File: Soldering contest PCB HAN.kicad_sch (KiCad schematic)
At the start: 11 parts, among them J1 Screw_Terminal_01x02, Q1 2N3904, Q2 2N3904

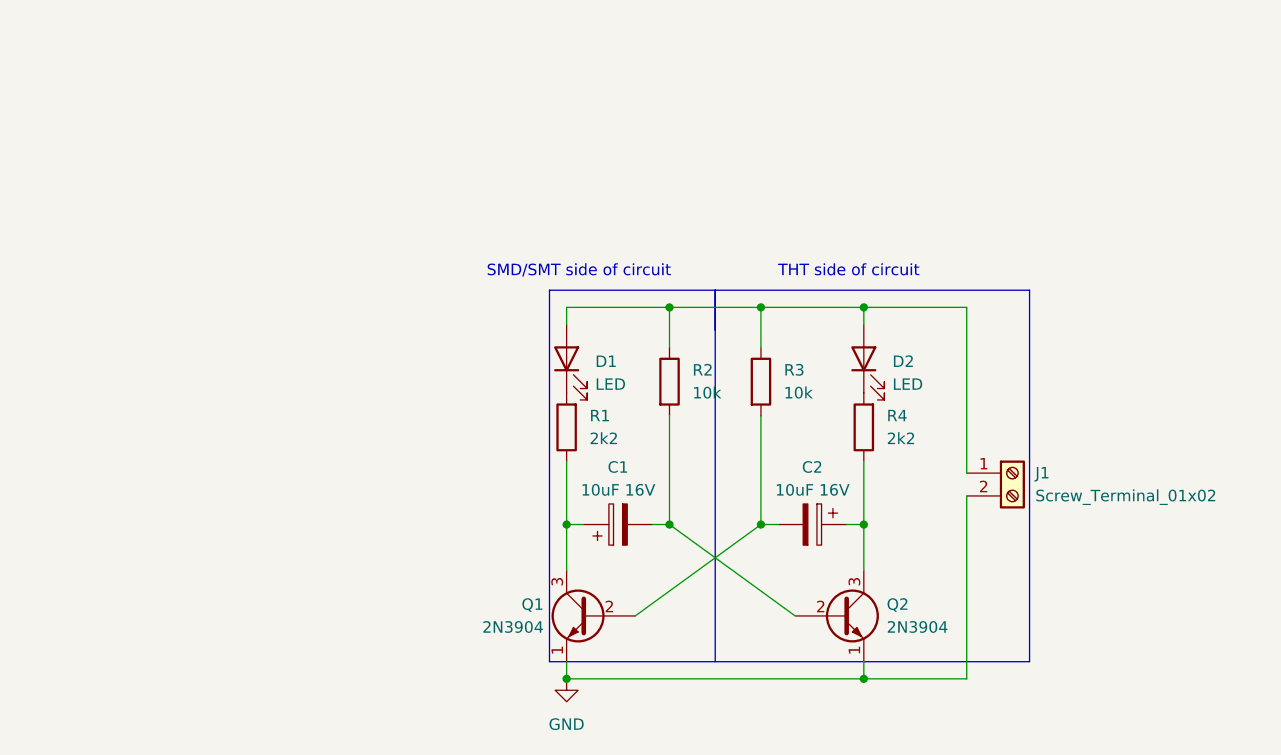
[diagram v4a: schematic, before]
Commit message: improved schematic board size
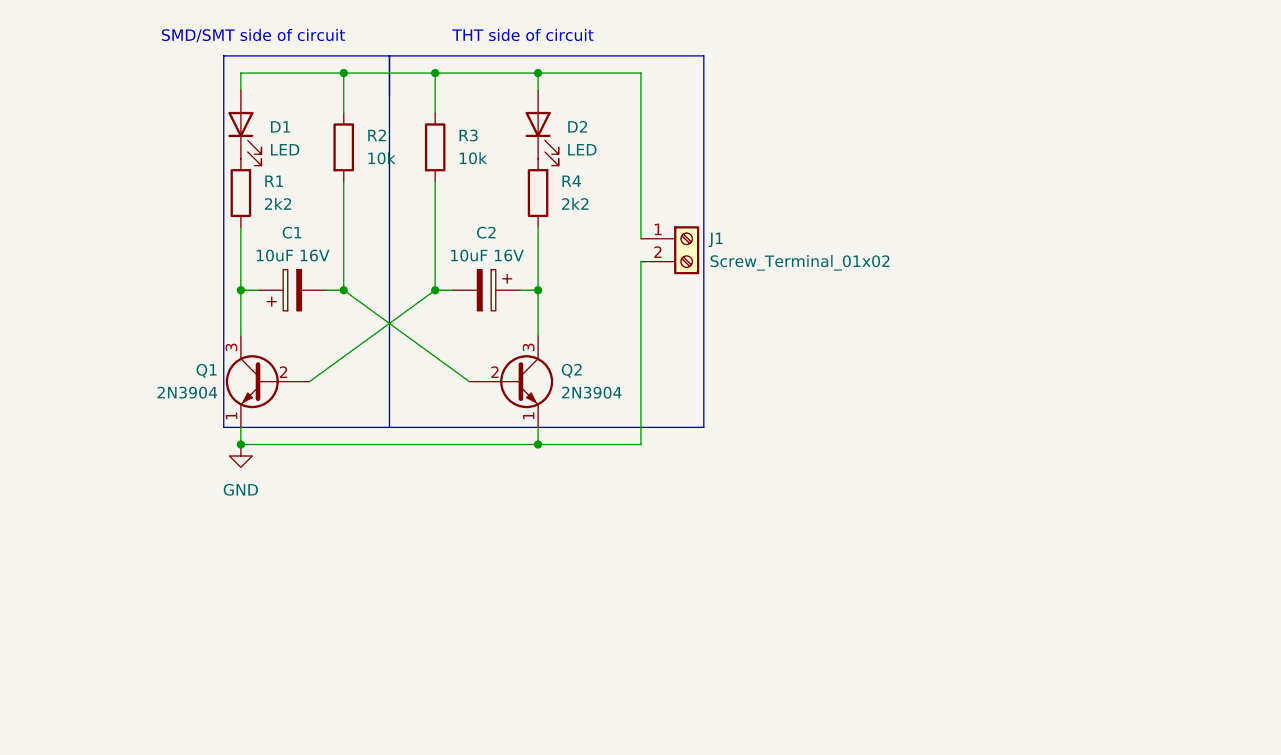
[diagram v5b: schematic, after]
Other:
- moved on the sheet: C1, C2, D1, D2, J1, Q1, Q2, R1, R2, R3, R4

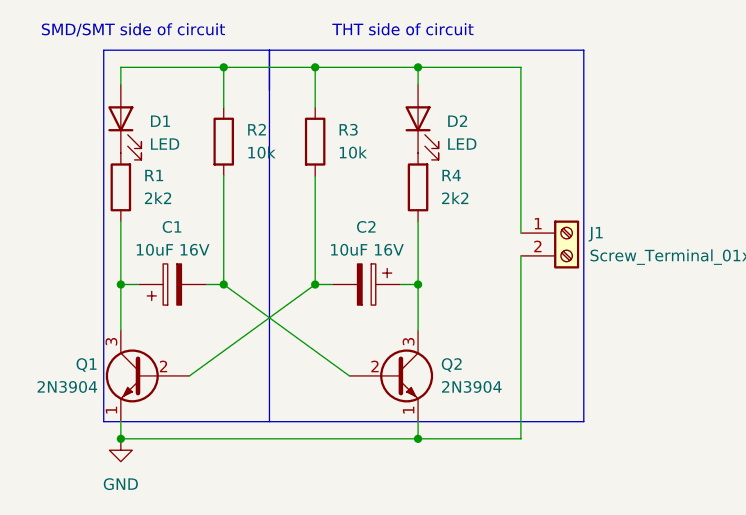
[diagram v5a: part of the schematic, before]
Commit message: replaced q1 footprint
replaced with sot23 handsolderable
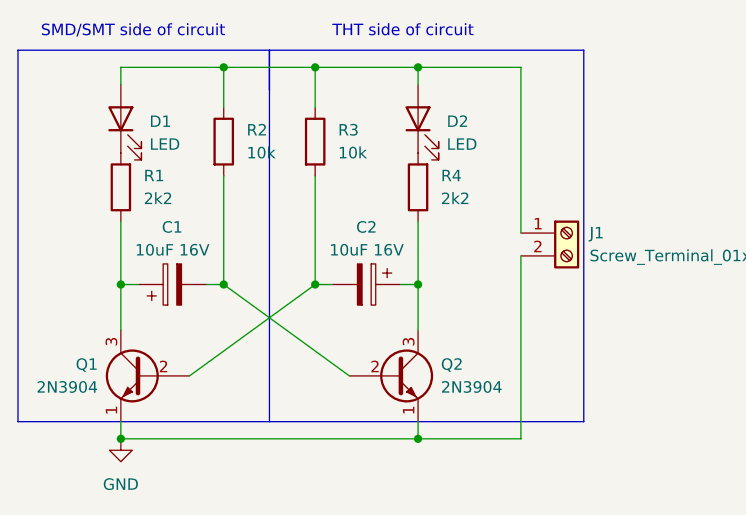
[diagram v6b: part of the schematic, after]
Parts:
- Q1: footprint Package_TO_SOT_THT:TO-92_Inline -> Package_TO_SOT_SMD:SOT-23_Handsoldering
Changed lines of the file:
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@@
   (junction (at 89.535 73.025) (diameter 0) (color 0 0 0 0)
   )
-  (polyline (pts (xy 94.615 46.99) (xy 76.2 46.99))
+  (polyline (pts (xy 94.615 46.99) (xy 66.675 46.99))
     (stroke (width 0) (type default) (color 0 0 0 0))
   )
@@
     (stroke (width 0) (type default) (color 0 0 0 0))
   )
-  (polyline (pts (xy 76.2 88.265) (xy 129.54 88.265))
+  (polyline (pts (xy 66.675 88.265) (xy 129.54 88.265))
     (stroke (width 0) (type default) (color 0 0 0 0))
   )
@@
     (stroke (width 0) (type default) (color 0 0 0 0))
   )
-  (polyline (pts (xy 76.2 46.99) (xy 76.2 88.265))
+  (polyline (pts (xy 66.675 46.99) (xy 66.675 88.265))
     (stroke (width 0) (type default) (color 0 0 0 0))
   )
@@
       (effects (font (size 1.27 1.27)) (justify left))
     )
-    (property "Footprint" "Package_TO_SOT_THT:TO-92_Inline" (id 2) (at 75.565 85.09 0)
+    (property "Footprint" "Package_TO_SOT_SMD:SOT-23_Handsoldering" (id 2) (at 75.565 85.09 0)
       (effects (font (size 1.27 1.27) italic) (justify left) hide)
     )
@@
     )
     (path "/6b424259-f8a0-4482-996c-adc9565aa863"
-      (reference "Q1") (unit 1) (value "2N3904") (footprint "Package_TO_SOT_THT:TO-92_Inline")
+      (reference "Q1") (unit 1) (value "2N3904") (footprint "Package_TO_SOT_SMD:SOT-23_Handsoldering")
     )
     (path "/0fd58cd3-0637-4e39-b339-0859c358a065"

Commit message: changed r3 footprint
smaller, so it's clear that it has to be soldered vertically
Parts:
- Q2: footprint Package_TO_SOT_THT:TO-92_Inline -> Package_TO_SOT_THT:TO-92_Inline_Wide
- R3: footprint Resistor_THT:R_Axial_DIN0207_L6.3mm_D2.5mm_P5.08mm_Vertical -> Resistor_THT:R_Axial_DIN0204_L3.6mm_D1.6mm_P2.54mm_Vertical
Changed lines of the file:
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@@
       (effects (font (size 1.27 1.27)) (justify left))
     )
-    (property "Footprint" "Package_TO_SOT_THT:TO-92_Inline" (id 2) (at 113.665 85.09 0)
+    (property "Footprint" "Package_TO_SOT_THT:TO-92_Inline_Wide" (id 2) (at 113.665 85.09 0)
       (effects (font (size 1.27 1.27) italic) (justify left) hide)
     )
@@
       (effects (font (size 1.27 1.27)) (justify left))
     )
-    (property "Footprint" "Resistor_THT:R_Axial_DIN0207_L6.3mm_D2.5mm_P5.08mm_Vertical" (id 2) (at 97.917 57.15 90)
+    (property "Footprint" "Resistor_THT:R_Axial_DIN0204_L3.6mm_D1.6mm_P2.54mm_Vertical" (id 2) (at 97.917 57.15 90)
       (effects (font (size 1.27 1.27)) hide)
     )
@@
     )
     (path "/0fd58cd3-0637-4e39-b339-0859c358a065"
-      (reference "Q2") (unit 1) (value "2N3904") (footprint "Package_TO_SOT_THT:TO-92_Inline")
+      (reference "Q2") (unit 1) (value "2N3904") (footprint "Package_TO_SOT_THT:TO-92_Inline_Wide")
     )
     (path "/d18fc897-0878-42f5-b8a2-449363703de6"
@@
     )
     (path "/5fd75fa8-c971-4180-8d4d-419bf5fd463a"
-      (reference "R3") (unit 1) (value "10k") (footprint "Resistor_THT:R_Axial_DIN0207_L6.3mm_D2.5mm_P5.08mm_Vertical")
+      (reference "R3") (unit 1) (value "10k") (footprint "Resistor_THT:R_Axial_DIN0204_L3.6mm_D1.6mm_P2.54mm_Vertical")
     )
     (path "/22a04216-54cb-44fe-9b76-e181b36e1a9f"

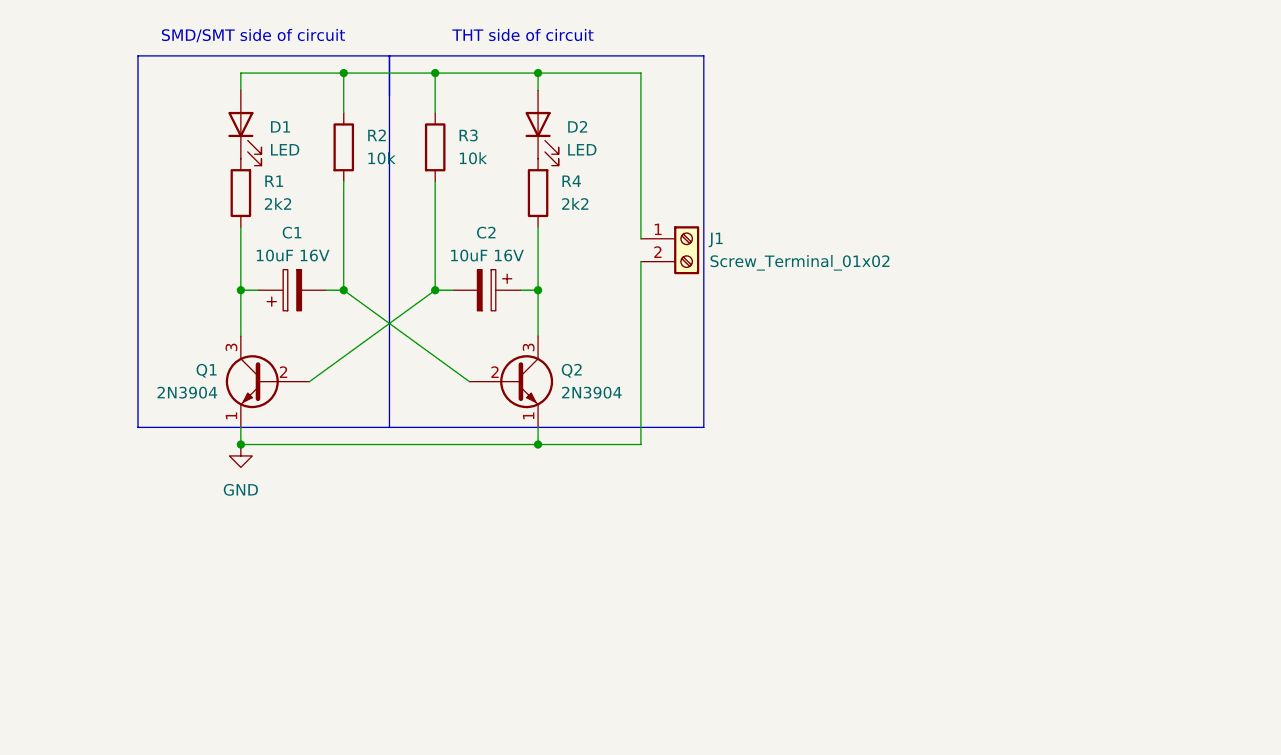
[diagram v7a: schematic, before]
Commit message: add bat, switch changed schematic
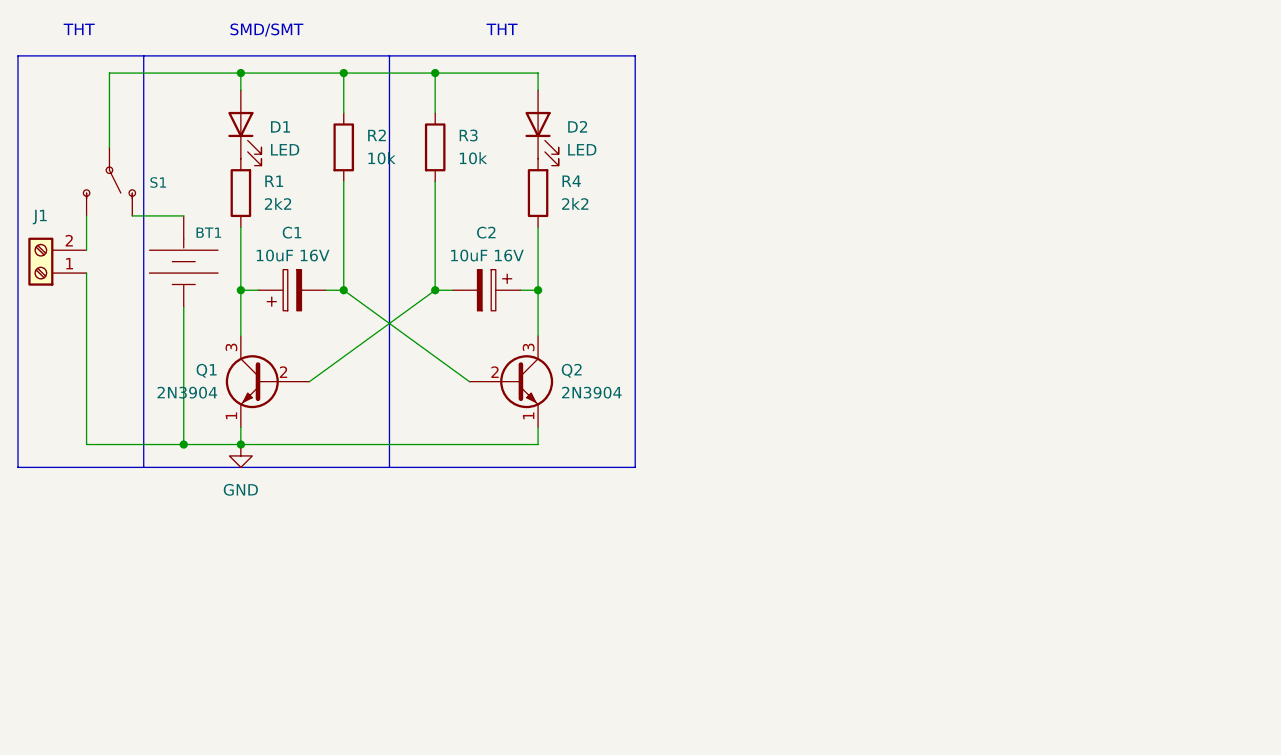
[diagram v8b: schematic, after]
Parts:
- added BT1: BATTERY-6.8MM_SMD, Battery:BatteryHolder_Keystone_3002_1x2032, symbol SparkFun-Batteries:BATTERY-6.8MM_SMD
- added S1: SWITCH-SPDT-PTH-11.6X4.0MM-KIT, SnapEDA Library:SW_1825159-1, symbol SparkFun-Switches:SWITCH-SPDT-PTH-11.6X4.0MM-KIT
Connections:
- net GND: now also J1.1 (Pin_1), BT1.-; no longer J1.2 (Pin_2)
- net at D1.2 (A), D2.2 (A), R2.1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: now also S1.2 (P); no longer J1.1 (Pin_1)
- new net: J1.2 (Pin_2), S1.3 (S)
- new net: BT1.+, S1.1 (O)
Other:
- note added: "SMD/SMT"
- note added: "THT"
- note removed: "SMD/SMT side of circuit"
- note removed: "THT side of circuit"
- moved on the sheet: J1
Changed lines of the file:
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@@
   (junction (at 78.105 90.17) (diameter 0) (color 0 0 0 0)
   )
-  (junction (at 111.125 90.17) (diameter 0) (color 0 0 0 0)
+  (junction (at 78.105 48.895) (diameter 0) (color 0 0 0 0)
   )
   (junction (at 111.125 73.025) (diameter 0) (color 0 0 0 0)
@@
   (junction (at 99.695 48.895) (diameter 0) (color 0 0 0 0)
   )
+  (junction (at 71.755 90.17) (diameter 0) (color 0 0 0 0)
+  )
   (junction (at 89.535 48.895) (diameter 0) (color 0 0 0 0)
   )
   (junction (at 99.695 73.025) (diameter 0) (color 0 0 0 0)
   )
-  (junction (at 111.125 48.895) (diameter 0) (color 0 0 0 0)
-  )
   (junction (at 89.535 73.025) (diameter 0) (color 0 0 0 0)
   )
-  (polyline (pts (xy 94.615 46.99) (xy 66.675 46.99))
-    (stroke (width 0) (type default) (color 0 0 0 0))
-  )
-  (polyline (pts (xy 94.615 88.265) (xy 94.615 46.99))
-    (stroke (width 0) (type default) (color 0 0 0 0))
-  )
-  (wire (pts (xy 122.555 69.85) (xy 122.555 90.17))
+  (wire (pts (xy 60.96 68.58) (xy 60.96 64.77))
+    (stroke (width 0) (type default) (color 0 0 0 0))
+  )
+  (wire (pts (xy 71.755 74.93) (xy 71.755 90.17))
+    (stroke (width 0) (type default) (color 0 0 0 0))
+  )
+  (polyline (pts (xy 94.615 46.99) (xy 53.34 46.99))
+    (stroke (width 0) (type default) (color 0 0 0 0))
+  )
+  (polyline (pts (xy 94.615 92.71) (xy 94.615 46.99))
     (stroke (width 0) (type default) (color 0 0 0 0))
   )
@@
     (stroke (width 0) (type default) (color 0 0 0 0))
   )
-  (polyline (pts (xy 94.615 46.99) (xy 94.615 51.435))
-    (stroke (width 0) (type default) (color 0 0 0 0))
-  )
   (wire (pts (xy 99.695 73.025) (xy 101.6 73.025))
     (stroke (width 0) (type default) (color 0 0 0 0))
@@
     (stroke (width 0) (type default) (color 0 0 0 0))
   )
+  (polyline (pts (xy 67.31 92.71) (xy 67.31 46.99))
+    (stroke (width 0) (type default) (color 0 0 0 0))
+  )
+  (wire (pts (xy 60.96 71.12) (xy 60.96 90.17))
+    (stroke (width 0) (type default) (color 0 0 0 0))
+  )
   (wire (pts (xy 80.01 73.025) (xy 78.105 73.025))
     (stroke (width 0) (type default) (color 0 0 0 0))
@@
     (stroke (width 0) (type default) (color 0 0 0 0))
   )
+  (wire (pts (xy 66.04 64.77) (xy 71.755 64.77))
+    (stroke (width 0) (type default) (color 0 0 0 0))
+  )
+  (wire (pts (xy 71.755 90.17) (xy 78.105 90.17))
+    (stroke (width 0) (type default) (color 0 0 0 0))
+  )
   (wire (pts (xy 78.105 90.17) (xy 78.105 88.265))
     (stroke (width 0) (type default) (color 0 0 0 0))
   )
-  (wire (pts (xy 122.555 90.17) (xy 111.125 90.17))
+  (wire (pts (xy 63.5 48.895) (xy 78.105 48.895))
     (stroke (width 0) (type default) (color 0 0 0 0))
   )
@@
     (stroke (width 0) (type default) (color 0 0 0 0))
   )
-  (polyline (pts (xy 66.675 88.265) (xy 129.54 88.265))
-    (stroke (width 0) (type default) (color 0 0 0 0))
-  )
-  (wire (pts (xy 122.555 48.895) (xy 122.555 67.31))
+  (polyline (pts (xy 53.34 92.71) (xy 121.92 92.71))
+    (stroke (width 0) (type default) (color 0 0 0 0))
+  )
+  (wire (pts (xy 60.96 90.17) (xy 71.755 90.17))
     (stroke (width 0) (type default) (color 0 0 0 0))
   )
@@
     (stroke (width 0) (type default) (color 0 0 0 0))
   )
-  (polyline (pts (xy 66.675 46.99) (xy 66.675 88.265))
+  (polyline (pts (xy 53.34 46.99) (xy 53.34 92.71))
     (stroke (width 0) (type default) (color 0 0 0 0))
   )
@@
     (stroke (width 0) (type default) (color 0 0 0 0))
   )
-  (wire (pts (xy 111.125 48.895) (xy 122.555 48.895))
-    (stroke (width 0) (type default) (color 0 0 0 0))
-  )
-  (polyline (pts (xy 129.54 46.99) (xy 94.615 46.99))
+  (polyline (pts (xy 121.92 46.99) (xy 94.615 46.99))
     (stroke (width 0) (type default) (color 0 0 0 0))
   )
@@
     (stroke (width 0) (type default) (color 0 0 0 0))
   )
+  (wire (pts (xy 63.5 57.15) (xy 63.5 48.895))
+    (stroke (width 0) (type default) (color 0 0 0 0))
+  )
   (wire (pts (xy 78.105 90.17) (xy 111.125 90.17))
     (stroke (width 0) (type default) (color 0 0 0 0))
   )
-  (polyline (pts (xy 129.54 88.265) (xy 129.54 46.99))
+  (polyline (pts (xy 121.92 92.71) (xy 121.92 46.99))
     (stroke (width 0) (type default) (color 0 0 0 0))
   )
@@
     (stroke (width 0) (type default) (color 0 0 0 0))
   )
-  (text "SMD/SMT side of circuit\n" (at 69.215 45.72 0)
+  (text "SMD/SMT \n" (at 76.835 45.085 0)
     (effects (font (size 1.27 1.27)) (justify left bottom))
   )
-  (text "THT side of circuit\n" (at 101.6 45.72 0)
+  (text "THT" (at 105.41 45.085 0)
+    (effects (font (size 1.27 1.27)) (justify left bottom))
+  )
+  (text "THT" (at 58.42 45.085 0)
     (effects (font (size 1.27 1.27)) (justify left bottom))
   )
@@
     (pin "3")
   )
-  (symbol (lib_id "Connector:Screw_Terminal_01x02") (at 127.635 67.31 0) (unit 1)
-    (in_bom yes) (on_board yes) (fields_autoplaced)
-    (property "Reference" "J1" (id 0) (at 130.175 67.3099 0)
-      (effects (font (size 1.27 1.27)) (justify left))
-    )
-    (property "Value" "Screw_Terminal_01x02" (id 1) (at 130.175 69.8499 0)
-      (effects (font (size 1.27 1.27)) (justify left))
-    )
-    (property "Footprint" "TerminalBlock:TerminalBlock_bornier-2_P5.08mm" (id 2) (at 127.635 67.31 0)
-      (effects (font (size 1.27 1.27)) hide)
-    )
-    (property "Datasheet" "~" (id 3) (at 127.635 67.31 0)
+  (symbol (lib_id "Connector:Screw_Terminal_01x02") (at 55.88 71.12 180) (unit 1)
+    (in_bom yes) (on_board yes) (fields_autoplaced)
+    (property "Reference" "J1" (id 0) (at 55.88 64.77 0))
+    (property "Value" "Screw_Terminal_01x02" (id 1) (at 54.6101 73.66 90)
+      (effects (font (size 1.27 1.27)) (justify left) hide)
+    )
+    (property "Footprint" "TerminalBlock:TerminalBlock_bornier-2_P5.08mm" (id 2) (at 55.88 71.12 0)
+      (effects (font (size 1.27 1.27)) hide)
+    )
+    (property "Datasheet" "~" (id 3) (at 55.88 71.12 0)
       (effects (font (size 1.27 1.27)) hide)
     )
@@
     (pin "1")
     (pin "2")
+  )
+  (symbol (lib_id "SparkFun-Batteries:BATTERY-6.8MM_SMD") (at 71.755 69.85 270) (unit 1)
+    (in_bom yes) (on_board yes)
+    (property "Reference" "BT1" (id 0) (at 73.025 66.675 90)
+      (effects (font (size 1.143 1.143)) (justify left))
+    )
+    (property "Value" "BATTERY-6.8MM_SMD" (id 1) (at 76.835 69.85 90)
+      (effects (font (size 1.143 1.143)) (justify left) hide)
+    )
+    (property "Footprint" "Battery:BatteryHolder_Keystone_3002_1x2032" (id 2) (at 78.105 69.85 0)
+      (effects (font (size 0.508 0.508)) hide)
+    )
+    (property "Datasheet" "" (id 3) (at 71.755 69.85 0)
+      (effects (font (size 1.27 1.27)) hide)
+    )
+    (property "Field4" "BATT-13734" (id 4) (at 76.835 73.025 90)
+      (effects (font (size 1.524 1.524)) (justify left) hide)
+    )
+    (property "Purpose" "C2032" (id 5) (at 85.725 68.58 90)
+      (effects (font (size 1.27 1.27)) hide)
+    )
+    (pin "+")
+    (pin "-")
   )
   (symbol (lib_id "Device:C_Polarized") (at 83.82 73.025 90) (unit 1)
@@
     (pin "2")
   )
+  (symbol (lib_id "SparkFun-Switches:SWITCH-SPDT-PTH-11.6X4.0MM-KIT") (at 63.5 59.69 270) (unit 1)
+    (in_bom yes) (on_board yes) (fields_autoplaced)
+    (property "Reference" "S1" (id 0) (at 67.945 61.0997 90)
+      (effects (font (size 1.143 1.143)) (justify left))
+    )
+    (property "Value" "SWITCH-SPDT-PTH-11.6X4.0MM-KIT" (id 1) (at 57.785 61.0997 0)
+      (effects (font (size 1.143 1.143)) hide)
+    )
+    (property "Footprint" "SnapEDA Library:SW_1825159-1" (id 2) (at 69.85 59.69 0)
+      (effects (font (size 0.508 0.508)) hide)
+    )
+    (property "Datasheet" "" (id 3) (at 63.5 59.69 0)
+      (effects (font (size 1.27 1.27)) hide)
+    )
+    (property "Field4" "SWCH-08261" (id 4) (at 59.055 61.0997 0)
+      (effects (font (size 1.524 1.524)) hide)
+    )
+    (pin "1")
+    (pin "2")
+    (pin "3")
+  )
   (symbol (lib_id "Transistor_BJT:2N3904") (at 80.645 83.185 0) (mirror y) (unit 1)
     (in_bom yes) (on_board yes) (fields_autoplaced)
@@
       (reference "#PWR01") (unit 1) (value "GND") (footprint "")
     )
+    (path "/44a5ce8e-2c11-4619-8ce9-b752075d2088"
+      (reference "BT1") (unit 1) (value "BATTERY-6.8MM_SMD") (footprint "Battery:BatteryHolder_Keystone_3002_1x2032")
+    )
     (path "/5c87c882-b6f1-48af-94eb-8b3a9c0bcf0b"
       (reference "C1") (unit 1) (value "10uF 16V") (footprint "Capacitor_SMD:C_1206_3216Metric_Pad1.33x1.80mm_HandSolder")
@@
       (reference "R4") (unit 1) (value "2k2") (footprint "Resistor_THT:R_Axial_DIN0207_L6.3mm_D2.5mm_P7.62mm_Horizontal")
     )
-  )
+    (path "/6502d947-661b-4d45-91f3-16aac5eae88a"
+      (reference "S1") (unit 1) (value "SWITCH-SPDT-PTH-11.6X4.0MM-KIT") (footprint "SnapEDA Library:SW_1825159-1")
+    )
+  )
